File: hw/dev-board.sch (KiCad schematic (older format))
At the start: 65 parts, among them CON1 BARREL_JACK, IC1 FDG6331L, P1 USB_OTG, P10 CONN_01X06, P11 CONN_01X08, P2 CONN_02X03_ICSP, P3 CONN_02X03, P4 CONN_02X03_ICSP, P5 CONN_01X08, P6 CONN_02X03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

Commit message: Fix layout.
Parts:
- renumbered IC1 to U11
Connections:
- net D+: now reaches R3.1, U3.29 (D+)
- net D-: now reaches R4.2, U3.30 (D-)
- net D_N: now reaches P1.2 (D-), R4.1, VR1.1
- net D_P: now reaches P1.3 (D+), R3.2, VR2.1
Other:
- moved on the sheet: F1, L1, P1, R3, R4, VR2

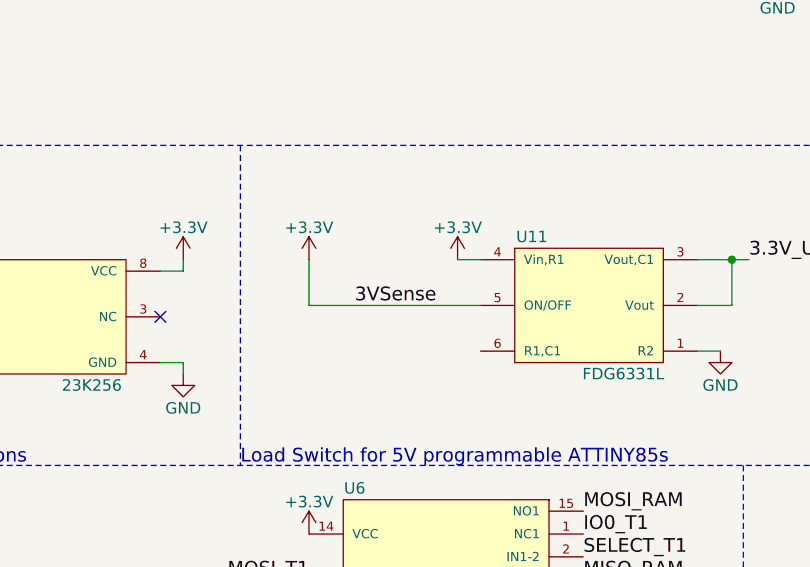
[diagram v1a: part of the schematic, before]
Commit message: No major changes. PCB is 50% routed with clear vert/horiz pattern. This is just a restore point.
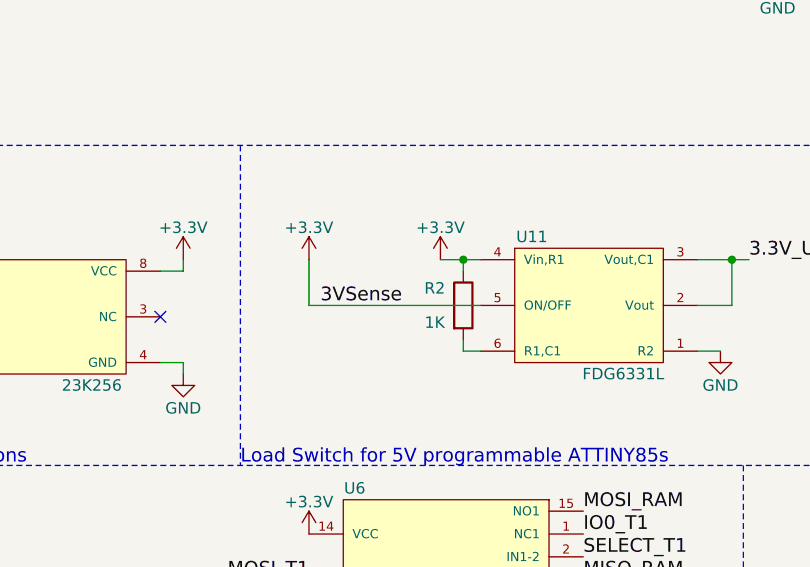
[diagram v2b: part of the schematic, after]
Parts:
- added R2: 1K, Resistors_SMD:R_0603, symbol R
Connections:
- net +3V3: now also R2.1
- net at U11.6 (R1,C1): now also R2.2

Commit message: Add footprint for 4 bit level shifter.
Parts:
- removed U8: 74LVCH1T45, Housings_SSOP:MSOP-8_3x3mm_Pitch0.65mm, symbol 74LVCH1T45
- added U8: FXMA2104, symbol FXMA2104
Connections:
- net +3V3: now also U8.1 (VCCB)
- net +5V: now also U8.2 (VCCA)
- net AD4/SCK1: now also U8.4 (A1)
- net GND: now also U8.7 (GND), U8.8 (OE)
- net MISO_T1: now also U5.5 (PB0(MOSI/DI/SDA/AIN0/OC0A/OC1A/AREF/PCINT0)); no longer U5.6 (PB1(MISO/DO/AIN1/OC0B/OC1A/PCINT1))
- net MISO_T2: now also U9.5 (PB0(MOSI/DI/SDA/AIN0/OC0A/OC1A/AREF/PCINT0)); no longer U9.6 (PB1(MISO/DO/AIN1/OC0B/OC1A/PCINT1))
- net MOSI1_328: now also U8.5 (A2)
- net MOSI_RAM: now also U8.11 (B1)
- net MOSI_T1: now also U5.6 (PB1(MISO/DO/AIN1/OC0B/OC1A/PCINT1)); no longer U5.5 (PB0(MOSI/DI/SDA/AIN0/OC0A/OC1A/AREF/PCINT0))
- net MOSI_T2: now also U9.6 (PB1(MISO/DO/AIN1/OC0B/OC1A/PCINT1)); no longer U9.5 (PB0(MOSI/DI/SDA/AIN0/OC0A/OC1A/AREF/PCINT0))
- net SCK_RAM: now also U8.10 (B2)
- net ~SS~: now also U8.9 (B3)
- net ~SS~_328: now also U8.6 (A3)
- no-connect marks 18 -> 20
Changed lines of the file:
@@
 Text Label 7900 8000 0    60   ~ 0
 MOSI_T1
-Text Label 7250 8800 2    60   ~ 0
+Text Label 7250 8700 2    60   ~ 0
 MISO_T1
 Text Label 7250 8900 2    60   ~ 0
 SCK_T1
-Text Label 7250 8700 2    60   ~ 0
+Text Label 7250 8800 2    60   ~ 0
 MOSI_T1
 Text Label 8300 7850 0    60   ~ 0
@@
 Text Label 12550 8000 0    60   ~ 0
 MOSI_T2
-Text Label 11900 8800 2    60   ~ 0
+Text Label 11900 8700 2    60   ~ 0
 MISO_T2
 Text Label 11900 8900 2    60   ~ 0
 SCK_T2
-Text Label 11900 8700 2    60   ~ 0
+Text Label 11900 8800 2    60   ~ 0
 MOSI_T2
 Text Label 12950 7850 0    60   ~ 0
@@
 MOSI1_328
 $Comp
-L 74LVCH1T45 U8
-U 1 1 5763D0D6
-P 13100 6200
-F 0 "U8" H 12850 6450 50  0000 C CNN
-F 1 "74LVCH1T45" H 13250 5950 50  0000 C CNN
-F 2 "Housings_SSOP:MSOP-8_3x3mm_Pitch0.65mm" H 13100 5850 50  0001 C CIN
-F 3 "" H 13100 6200 50  0000 C CNN
-	1    13100 6200
-	1    0    0    -1
-$EndComp
-$Comp
 L GND #PWR049
 U 1 1 5763D4FE
-P 13600 6350
-F 0 "#PWR049" H 13600 6100 50  0001 C CNN
-F 1 "GND" H 13600 6200 50  0000 C CNN
-F 2 "" H 13600 6350 50  0000 C CNN
-F 3 "" H 13600 6350 50  0000 C CNN
-	1    13600 6350
+P 13650 6500
+F 0 "#PWR049" H 13650 6250 50  0001 C CNN
+F 1 "GND" H 13650 6350 50  0000 C CNN
+F 2 "" H 13650 6500 50  0000 C CNN
+F 3 "" H 13650 6500 50  0000 C CNN
+	1    13650 6500
 	1    0    0    -1
 $EndComp
@@
 L +5V #PWR050
 U 1 1 5763DB38
-P 12600 6050
-F 0 "#PWR050" H 12600 5900 50  0001 C CNN
-F 1 "+5V" H 12600 6190 50  0000 C CNN
-F 2 "" H 12600 6050 50  0000 C CNN
-F 3 "" H 12600 6050 50  0000 C CNN
-	1    12600 6050
+P 12550 5900
+F 0 "#PWR050" H 12550 5750 50  0001 C CNN
+F 1 "+5V" H 12550 6040 50  0000 C CNN
+F 2 "" H 12550 5900 50  0000 C CNN
+F 3 "" H 12550 5900 50  0000 C CNN
+	1    12550 5900
 	1    0    0    -1
 $EndComp
@@
 L GND #PWR051
 U 1 1 5763DDDD
-P 12600 6350
-F 0 "#PWR051" H 12600 6100 50  0001 C CNN
-F 1 "GND" H 12600 6200 50  0000 C CNN
-F 2 "" H 12600 6350 50  0000 C CNN
-F 3 "" H 12600 6350 50  0000 C CNN
-	1    12600 6350
-	1    0    0    -1
-$EndComp
-Text Label 12600 6150 2    60   ~ 0
+P 12550 6500
+F 0 "#PWR051" H 12550 6250 50  0001 C CNN
+F 1 "GND" H 12550 6350 50  0000 C CNN
+F 2 "" H 12550 6500 50  0000 C CNN
+F 3 "" H 12550 6500 50  0000 C CNN
+	1    12550 6500
+	1    0    0    -1
+$EndComp
+Text Label 12100 6150 0    60   ~ 0
 AD4/SCK1
-Text Label 12600 6250 2    60   ~ 0
+Text Label 12100 6250 0    60   ~ 0
 MOSI1_328
 $Comp
 L +3.3V #PWR052
 U 1 1 57641F59
-P 13600 6050
-F 0 "#PWR052" H 13600 5900 50  0001 C CNN
-F 1 "+3.3V" H 13600 6190 50  0000 C CNN
-F 2 "" H 13600 6050 50  0000 C CNN
-F 3 "" H 13600 6050 50  0000 C CNN
-	1    13600 6050
-	1    0    0    -1
-$EndComp
-Text Label 13600 6250 0    60   ~ 0
+P 13650 5900
+F 0 "#PWR052" H 13650 5750 50  0001 C CNN
+F 1 "+3.3V" H 13650 6040 50  0000 C CNN
+F 2 "" H 13650 5900 50  0000 C CNN
+F 3 "" H 13650 5900 50  0000 C CNN
+	1    13650 5900
+	1    0    0    -1
+$EndComp
+Text Label 14100 6250 2    60   ~ 0
 SCK_RAM
-Text Label 13600 6150 0    60   ~ 0
+Text Label 14100 6150 2    60   ~ 0
 MOSI_RAM
 $Comp
@@
 	1    0    0    -1
 $EndComp
-Text Label 11125 6000 0    60   ~ 0
+Text Label 11700 6000 2    60   ~ 0
 3.3V_UNSAFE
 $Comp
@@
 Wire Notes Line
 	2650 10250 1900 10250
-Wire Wire Line
-	10900 6000 11125 6000
 Wire Wire Line
 	10900 6200 11050 6200
@@
 	9875 6050 9875 6000
 Connection ~ 9875 6000
+$Comp
+L FXMA2104 U8
+U 1 1 57EC74B3
+P 13100 6200
+F 0 "U8" H 13000 6600 60  0000 C CNN
+F 1 "FXMA2104" H 13150 5800 60  0000 C CNN
+F 2 "" H 13100 5750 60  0001 C CNN
+F 3 "" H 13100 5750 60  0001 C CNN
+	1    13100 6200
+	1    0    0    -1
+$EndComp
+Wire Wire Line
+	13600 5950 13650 5950
+Wire Wire Line
+	13650 5950 13650 5900
+Wire Wire Line
+	13600 6450 13650 6450
+Wire Wire Line
+	13650 6450 13650 6500
+Wire Wire Line
+	12550 6500 12550 6450
+Wire Wire Line
+	12550 6450 12600 6450
+Wire Wire Line
+	12100 6150 12600 6150
+Wire Wire Line
+	12100 6250 12600 6250
+Wire Wire Line
+	13600 6150 14100 6150
+Wire Wire Line
+	13600 6250 14100 6250
+Text Label 12100 6350 0    60   ~ 0
+~SS~_328
+Wire Wire Line
+	12100 6350 12600 6350
+Wire Wire Line
+	10900 6000 11700 6000
+Text Label 14100 6350 2    60   ~ 0
+~SS~
+Wire Wire Line
+	14100 6350 13600 6350
+Wire Wire Line
+	12550 5900 12550 5950
+Wire Wire Line
+	12550 5950 12600 5950
+NoConn ~ 12600 6050
+NoConn ~ 13600 6050
 $EndSCHEMATC
